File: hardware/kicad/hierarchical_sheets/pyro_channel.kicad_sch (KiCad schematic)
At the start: 20 parts, among them J2 Screw_Terminal_01x02, J3 282834-4, U2 ZXCT1110W5-7, U3 SI9926CDY

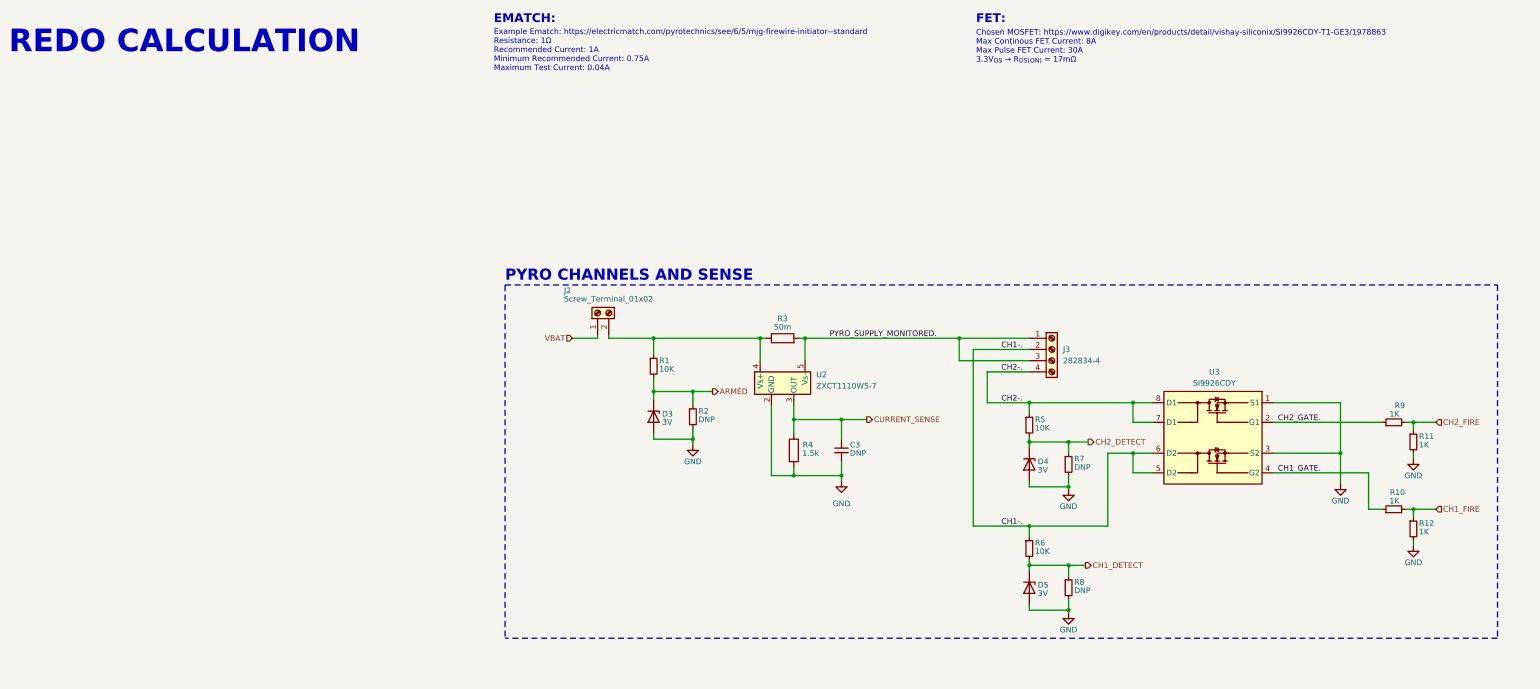
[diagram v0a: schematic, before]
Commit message: added pyro fuses
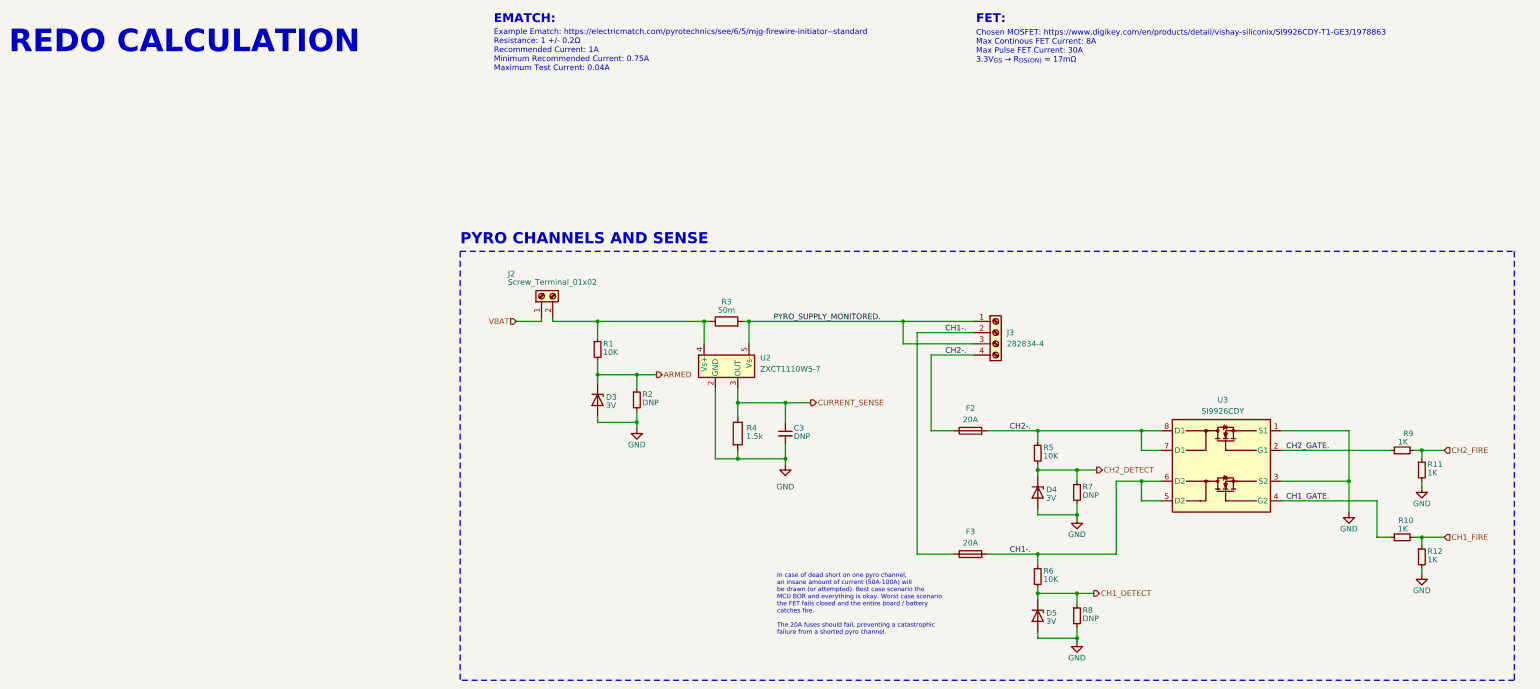
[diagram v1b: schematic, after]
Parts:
- added F2, F3: 20A, Resistor_SMD:R_1206_3216Metric, symbol Device:Fuse
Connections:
- net CH1-.: now also F3.1, F3.2
- net CH2-.: now also F2.1, F2.2
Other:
- note added: "Example Ematch: https://electricmatch.com/pyrotechnics/see/6/5/mjg-firewire-initiator--standard Resistance: 1 +/- 0.2Ω Recommended Current: 1A Minimum Recommended Current: 0.75A Maximum Test Current: 0.04A"
- note added: "In case of dead short on one pyro channel, an insane amount of current (50A-100A) will be drawn (or attempted). Best case scenario the MCU BOR and everything is okay. Worst case scenario the FET fails closed and the entire board / battery catches fire. The 20A fuses should fail, preventing a catastrophic failure from a shorted pyro channel."
- note removed: "Example Ematch: https://electricmatch.com/pyrotechnics/see/6/5/mjg-firewire-initiator--standard Resistance: 1Ω Recommended Current: 1A Minimum Recommended Current: 0.75A Maximum Test Current: 0.04A"
- moved on the sheet: C3, D3, D4, D5, J2, J3, R1, R10, R11, R12, R2, R3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

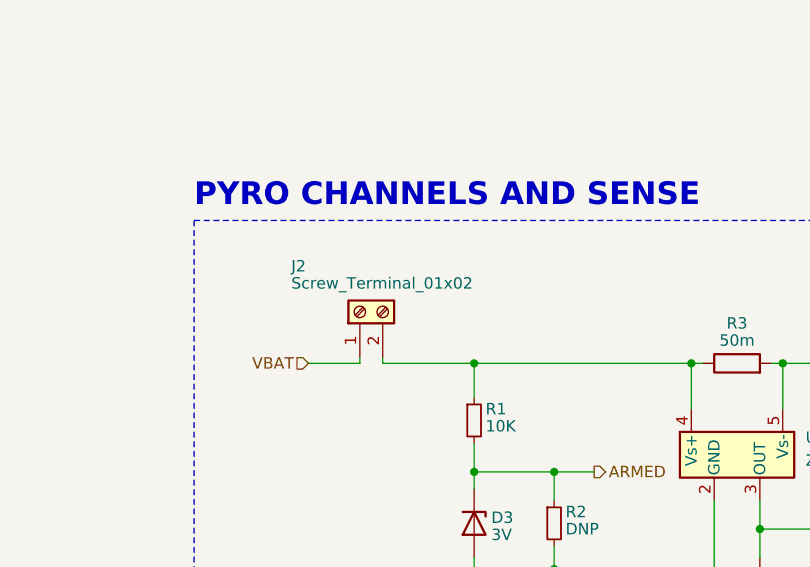
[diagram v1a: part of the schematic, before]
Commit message: all footprints have been fixed
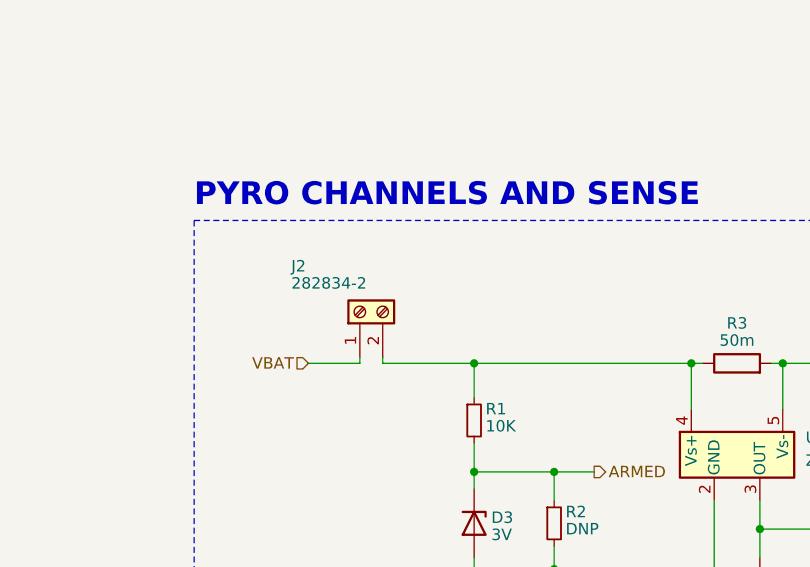
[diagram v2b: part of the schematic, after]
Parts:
- J2: value Screw_Terminal_01x02 -> 282834-2; footprint (none) -> TerminalBlock_TE-Connectivity:TerminalBlock_TE_282834-2_1x02_P2.54mm_Horizontal; Digikey (none) -> https://www.digikey.com/en/products/detail/te-connectivity-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
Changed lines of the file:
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@@
       (effects (font (size 1.27 1.27)) (justify right))
     )
-    (property "Value" "Screw_Terminal_01x02" (at 29.845 79.375 90)
+    (property "Value" "282834-2" (at 29.845 79.375 90)
       (effects (font (size 1.27 1.27)) (justify right))
     )
-    (property "Footprint" "" (at 37.465 82.55 0)
+    (property "Footprint" "TerminalBlock_TE-Connectivity:TerminalBlock_TE_282834-2_1x02_P2.54mm_Horizontal" (at 37.465 82.55 0)
       (effects (font (size 1.27 1.27)) hide)
     )
-    (property "Datasheet" "~" (at 37.465 82.55 0)
+    (property "Datasheet" "https://www.te.com/usa-en/product-282834-2.datasheet.pdf" (at 37.465 82.55 0)
       (effects (font (size 1.27 1.27)) hide)
     )
+    (property "Digikey" "https://www.digikey.com/en/products/detail/te-connectivity-amp-connectors/282834-2/1150135" (at 37.465 82.55 90)
+      (effects (font (size 1.27 1.27)) hide)
+    )

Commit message: formatting
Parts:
- renumbered F2 to F1, F3 to F2
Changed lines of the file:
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@@
   (symbol (lib_id "Device:Fuse") (at 134.62 113.03 90) (unit 1)
     (in_bom yes) (on_board yes) (dnp no) (fields_autoplaced)
-    (property "Reference" "F2" (at 134.62 107.95 90)
+    (property "Reference" "F1" (at 134.62 107.95 90)
       (effects (font (size 1.27 1.27)))
     )
@@
       (project "FC"
         (path "/54cce219-8b98-4e71-96c4-f9ee784aa3bc/047c0ef5-e762-41a7-bfd7-fdc982a27304"
-          (reference "F2") (unit 1)
+          (reference "F1") (unit 1)
         )
       )
@@
   (symbol (lib_id "Device:Fuse") (at 134.62 140.97 90) (unit 1)
     (in_bom yes) (on_board yes) (dnp no) (fields_autoplaced)
-    (property "Reference" "F3" (at 134.62 135.89 90)
+    (property "Reference" "F2" (at 134.62 135.89 90)
       (effects (font (size 1.27 1.27)))
     )
@@
       (project "FC"
         (path "/54cce219-8b98-4e71-96c4-f9ee784aa3bc/047c0ef5-e762-41a7-bfd7-fdc982a27304"
-          (reference "F3") (unit 1)
+          (reference "F2") (unit 1)
         )
       )

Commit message: formatting / exported pdf
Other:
- title: SRAD-FC -> Pyro Channels
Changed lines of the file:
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@@
   (paper "USLetter")
   (title_block
-    (title "SRAD-FC")
+    (title "Pyro Channels")
     (date "2023-04-27")
     (rev "0.1")

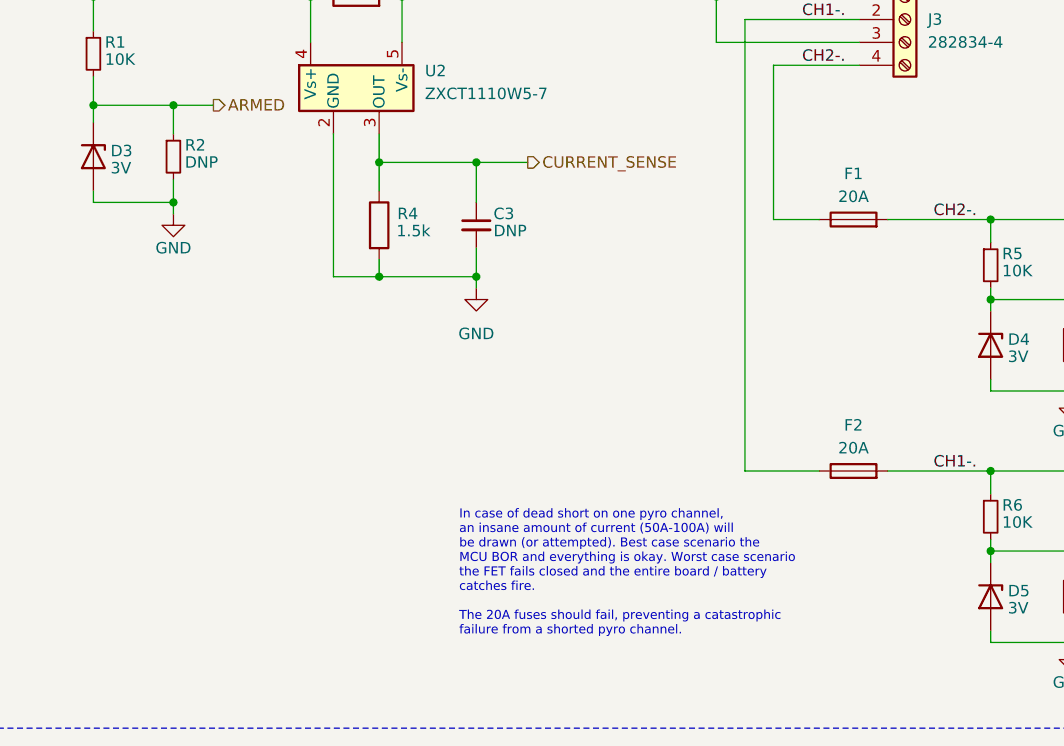
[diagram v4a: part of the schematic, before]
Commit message: changed fuse value
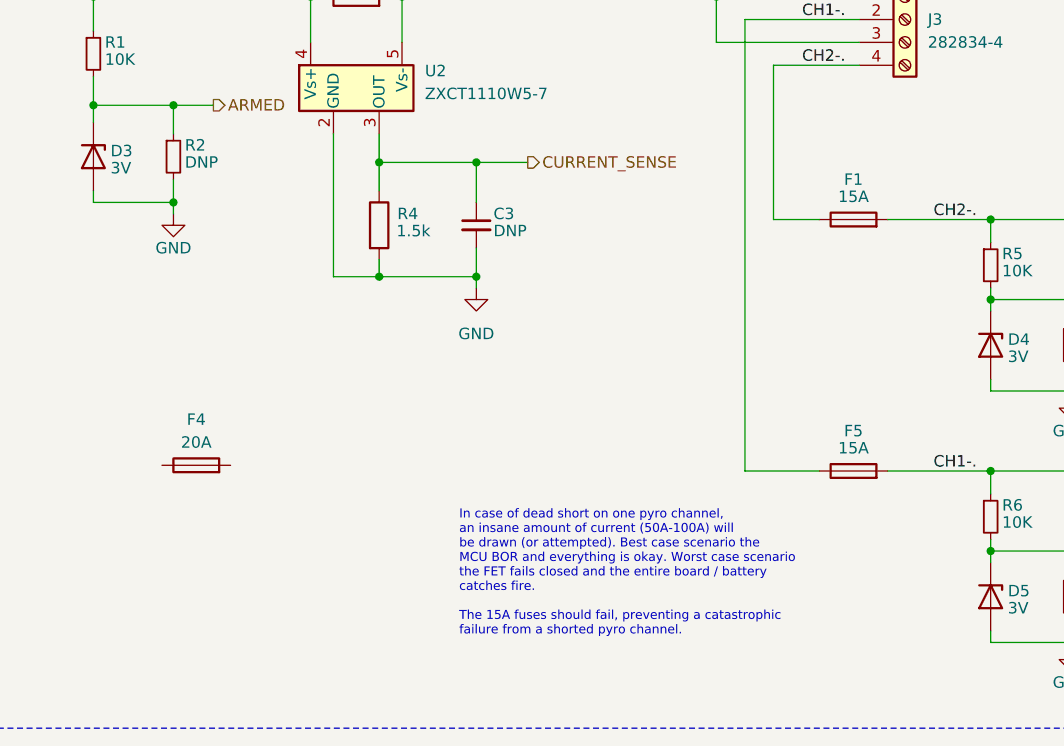
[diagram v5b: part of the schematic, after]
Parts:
- removed F2: 20A, Resistor_SMD:R_1206_3216Metric, symbol Device:Fuse
- added F4: 20A, Resistor_SMD:R_1206_3216Metric, symbol Device:Fuse
- added F5: 15A, Resistor_SMD:R_1206_3216Metric, symbol Device:Fuse
- F1: value 20A -> 15A; Digikey https://www.digikey.com/en/products/detail/bel-fuse-inc/0685H9200-01/5466708 -> https://www.digikey.com/en/products/detail/bel-fuse-inc/0685H9150-01/5466707
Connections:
- net CH1-.: now also F5.1, F5.2
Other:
- note added: "In case of dead short on one pyro channel, an insane amount of current (50A-100A) will be drawn (or attempted). Best case scenario the MCU BOR and everything is okay. Worst case scenario the FET fails closed and the entire board / battery catches fire. The 15A fuses should fail, preventing a catastrophic failure from a shorted pyro channel."
- note removed: "In case of dead short on one pyro channel, an insane amount of current (50A-100A) will be drawn (or attempted). Best case scenario the MCU BOR and everything is okay. Worst case scenario the FET fails closed and the entire board / battery catches fire. The 20A fuses should fail, preventing a catastrophic failure from a shorted pyro channel."
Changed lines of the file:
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@@
     (effects (font (size 2.52 2.52) (thickness 0.504) bold) (justify left bottom))
   )
-  (text "In case of dead short on one pyro channel, \nan insane amount of current (50A-100A) will\nbe drawn (or attempted). Best case scenario the \nMCU BOR and everything is okay. Worst case scenario\nthe FET fails closed and the entire board / battery\ncatches fire. \n\nThe 20A fuses should fail, preventing a catastrophic \nfailure from a shorted pyro channel.  "
+  (text "In case of dead short on one pyro channel, \nan insane amount of current (50A-100A) will\nbe drawn (or attempted). Best case scenario the \nMCU BOR and everything is okay. Worst case scenario\nthe FET fails closed and the entire board / battery\ncatches fire. \n\nThe 15A fuses should fail, preventing a catastrophic \nfailure from a shorted pyro channel.  "
     (at 90.805 159.385 0)
     (effects (font (size 1 1)) (justify left bottom))
@@
     )
   )
+  (symbol (lib_id "Device:Fuse") (at 61.595 140.335 90) (unit 1)
+    (in_bom yes) (on_board yes) (dnp no) (fields_autoplaced)
+    (property "Reference" "F4" (at 61.595 135.255 90)
+      (effects (font (size 1.27 1.27)))
+    )
+    (property "Value" "20A" (at 61.595 137.795 90)
+      (effects (font (size 1.27 1.27)))
+    )
+    (property "Footprint" "Resistor_SMD:R_1206_3216Metric" (at 61.595 142.113 90)
+      (effects (font (size 1.27 1.27)) hide)
+    )
+    (property "Datasheet" "https://www.belfuse.com/resources/datasheets/circuitprotection/ds-cp-c1h-series.pdf" (at 61.595 140.335 0)
+      (effects (font (size 1.27 1.27)) hide)
+    )
+    (property "Digikey" "https://www.digikey.com/en/products/detail/bel-fuse-inc/0685H9200-01/5466708" (at 61.595 140.335 0)
+      (effects (font (size 1.27 1.27)) hide)
+    )
+    (pin "1")
+    (pin "2")
+    (instances
+      (project "FC"
+        (path "/54cce219-8b98-4e71-96c4-f9ee784aa3bc/047c0ef5-e762-41a7-bfd7-fdc982a27304"
+          (reference "F4") (unit 1)
+        )
+      )
+    )
+  )
   (symbol (lib_id "Device:Fuse") (at 134.62 113.03 90) (unit 1)
-    (in_bom yes) (on_board yes) (dnp no) (fields_autoplaced)
-    (property "Reference" "F1" (at 134.62 107.95 90)
-      (effects (font (size 1.27 1.27)))
-    )
-    (property "Value" "20A" (at 134.62 110.49 90)
+    (in_bom yes) (on_board yes) (dnp no)
+    (property "Reference" "F1" (at 134.62 108.585 90)
+      (effects (font (size 1.27 1.27)))
+    )
+    (property "Value" "15A" (at 134.62 110.49 90)
       (effects (font (size 1.27 1.27)))
     )
@@
       (effects (font (size 1.27 1.27)) hide)
     )
-    (property "Digikey" "https://www.digikey.com/en/products/detail/bel-fuse-inc/0685H9200-01/5466708" (at 134.62 113.03 0)
+    (property "Digikey" "https://www.digikey.com/en/products/detail/bel-fuse-inc/0685H9150-01/5466707" (at 134.62 113.03 0)
       (effects (font (size 1.27 1.27)) hide)
     )
@@
   )
   (symbol (lib_id "Device:Fuse") (at 134.62 140.97 90) (unit 1)
-    (in_bom yes) (on_board yes) (dnp no) (fields_autoplaced)
-    (property "Reference" "F2" (at 134.62 135.89 90)
-      (effects (font (size 1.27 1.27)))
-    )
-    (property "Value" "20A" (at 134.62 138.43 90)
+    (in_bom yes) (on_board yes) (dnp no)
+    (property "Reference" "F5" (at 134.62 136.525 90)
+      (effects (font (size 1.27 1.27)))
+    )
+    (property "Value" "15A" (at 134.62 138.43 90)
       (effects (font (size 1.27 1.27)))
     )
@@
       (effects (font (size 1.27 1.27)) hide)
     )
-    (property "Digikey" "https://www.digikey.com/en/products/detail/bel-fuse-inc/0685H9200-01/5466708" (at 134.62 140.97 0)
-      (effects (font (size 1.27 1.27)) hide)
-    )
-    (pin "1")
-    (pin "2")
-    (instances
-      (project "FC"
-        (path "/54cce219-8b98-4e71-96c4-f9ee784aa3bc/047c0ef5-e762-41a7-bfd7-fdc982a27304"
-          (reference "F2") (unit 1)
-        )
-      )
+    (property "Digikey" "https://www.digikey.com/en/products/detail/bel-fuse-inc/0685H9150-01/5466707" (at 134.62 140.97 0)
+      (effects (font (size 1.27 1.27)) hide)
+    )
+    (pin "1")
+    (pin "2")
+    (instances
+      (project "FC"
+        (path "/54cce219-8b98-4e71-96c4-f9ee784aa3bc/047c0ef5-e762-41a7-bfd7-fdc982a27304"
+          (reference "F5") (unit 1)
+        )
+      )

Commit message: ready for pcb
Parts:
- removed F4: 20A, Resistor_SMD:R_1206_3216Metric, symbol Device:Fuse
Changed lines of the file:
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@@
-    )
-  )
-  (symbol (lib_id "Device:Fuse") (at 61.595 140.335 90) (unit 1)
-    (in_bom yes) (on_board yes) (dnp no) (fields_autoplaced)
-    (property "Reference" "F4" (at 61.595 135.255 90)
-      (effects (font (size 1.27 1.27)))
-    )
-    (property "Value" "20A" (at 61.595 137.795 90)
-      (effects (font (size 1.27 1.27)))
-    )
-    (property "Footprint" "Resistor_SMD:R_1206_3216Metric" (at 61.595 142.113 90)
-      (effects (font (size 1.27 1.27)) hide)
-    )
-    (property "Datasheet" "https://www.belfuse.com/resources/datasheets/circuitprotection/ds-cp-c1h-series.pdf" (at 61.595 140.335 0)
-      (effects (font (size 1.27 1.27)) hide)
-    )
-    (property "Digikey" "https://www.digikey.com/en/products/detail/bel-fuse-inc/0685H9200-01/5466708" (at 61.595 140.335 0)
-      (effects (font (size 1.27 1.27)) hide)
-    )
-    (pin "1")
-    (pin "2")
-    (instances
-      (project "FC"
-        (path "/54cce219-8b98-4e71-96c4-f9ee784aa3bc/047c0ef5-e762-41a7-bfd7-fdc982a27304"
-          (reference "F4") (unit 1)
-        )
-      )
     )
   )
